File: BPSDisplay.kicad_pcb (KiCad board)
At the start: 2 copper layers, 85 x 56 mm, 61 parts, among them J1 SWD, J3 CAN_Out, J4 CAN_Out, J5 CarPowerConnector, J6 CAN_LogicAnalyzer, J7 SPI0_LogicAnalyzer, J8 GEN_LogicAnalyzer, J9 USART_LogicAnalyzer, P1 Conn_02x20_Odd_Even, SW1 Reset, U1 STM32F413RHTx, U2 ADM3055E, U3 CDSOT23-T24CAN, U6 PDS1-S12-S5, U7 NCP1117-3.3_SOT223, Y1 8M

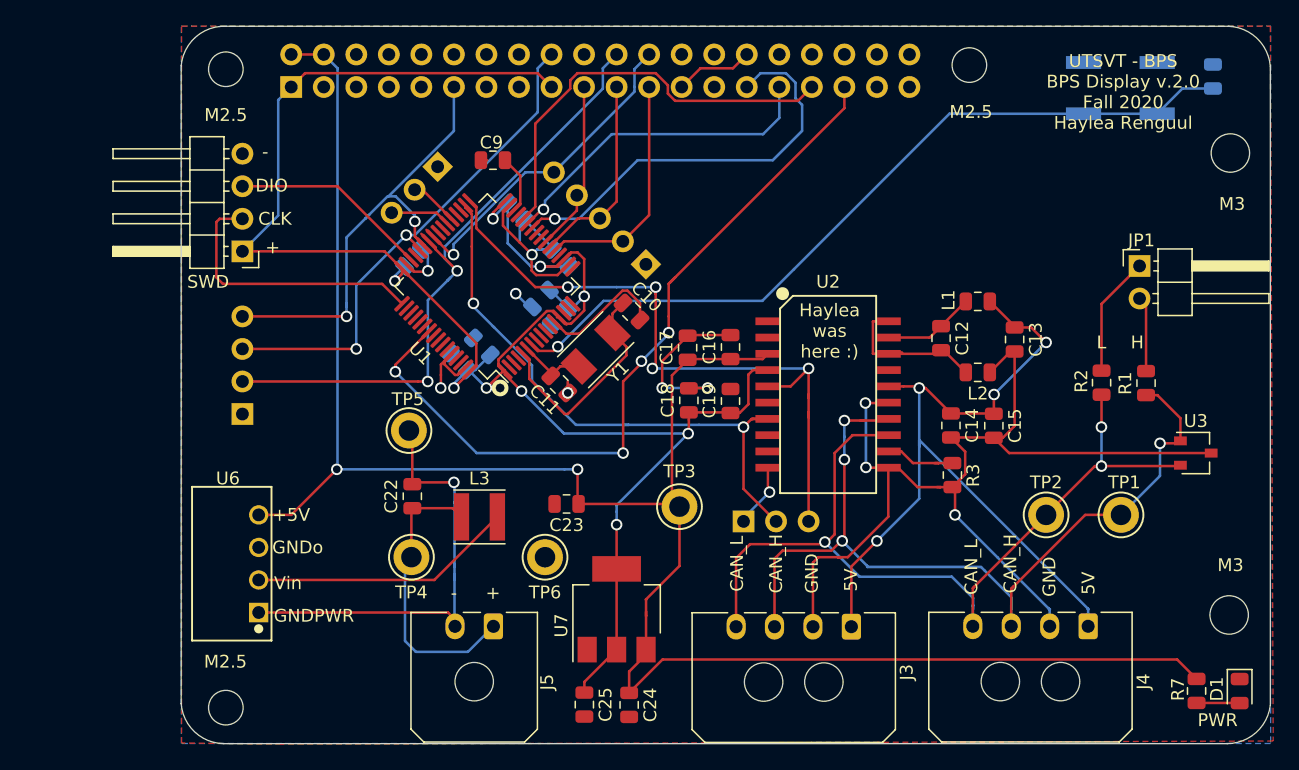
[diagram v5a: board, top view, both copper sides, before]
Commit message: Adds LED for supplementals, deletes unncessary files, and links all symbols to the submodule
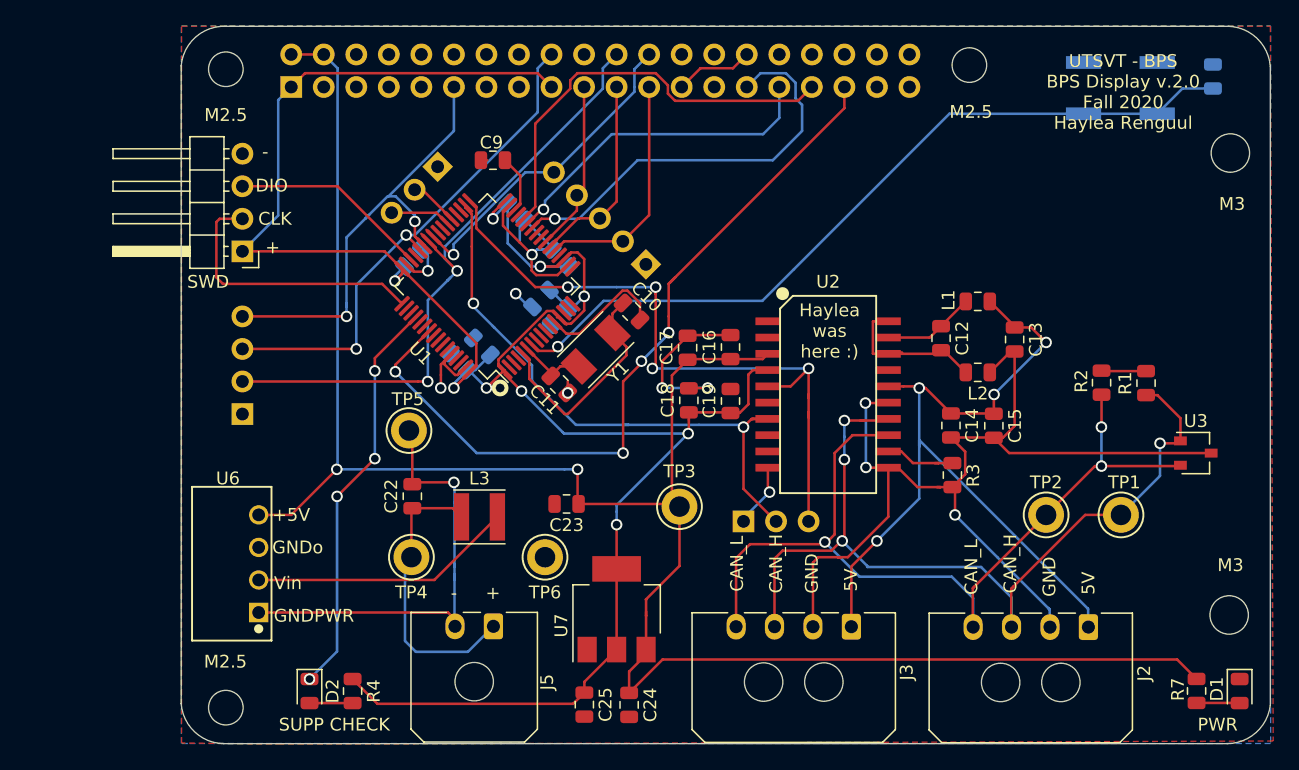
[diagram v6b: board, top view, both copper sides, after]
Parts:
- removed J4: CAN_Out, Connector_Molex:Molex_Micro-Fit_3.0_43650-0400_1x04_P3.00mm_Horizontal
- removed JP1: Termination Resistors, Connector_PinHeader_2.54mm:PinHeader_1x02_P2.54mm_Horizontal
- added D2: PowerOn, LED_SMD:LED_0805_2012Metric, F.Cu at (206.0, 156.9)
- added J2: CAN_Out, Connector_Molex:Molex_Micro-Fit_3.0_43650-0400_1x04_P3.00mm_Horizontal, F.Cu at (266.8, 151.9)
- added R4: 750, Resistor_SMD:R_0805_2012Metric, F.Cu at (209.4, 156.9)
- LOGO1: value Logo_Placeholder -> UTSVT
- LOGO2: value Logo_Placeholder -> Dr. Hallock
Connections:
- P1 pad 10: (no net) -> Net-(P1-Pad10)
- P1 pad 12: (no net) -> Net-(P1-Pad12)
- P1 pad 13: (no net) -> Net-(P1-Pad13)
- P1 pad 15: (no net) -> Net-(P1-Pad15)
- P1 pad 16: (no net) -> Net-(P1-Pad16)
- P1 pad 26: (no net) -> Net-(P1-Pad26)
- P1 pad 27: (no net) -> Net-(P1-Pad27)
- P1 pad 28: (no net) -> Net-(P1-Pad28)
- P1 pad 3: (no net) -> Net-(P1-Pad3)
- P1 pad 32: (no net) -> Net-(P1-Pad32)
- P1 pad 36: (no net) -> Net-(P1-Pad36)
- P1 pad 37: (no net) -> Net-(P1-Pad37)
- P1 pad 38: (no net) -> Net-(P1-Pad38)
- P1 pad 40: (no net) -> Net-(P1-Pad40)
- P1 pad 5: (no net) -> Net-(P1-Pad5)
- P1 pad 7: (no net) -> Net-(P1-Pad7)
- P1 pad 8: (no net) -> Net-(P1-Pad8)
- R1 pad 1: /CAN/TERM_H -> Net-(R1-Pad1)
- R2 pad 1: /CAN/TERM_L -> Net-(R1-Pad1)
- U1 pad 10: (no net) -> Net-(U1-Pad10)
- U1 pad 11: (no net) -> Net-(U1-Pad11)
- U1 pad 14: (no net) -> Net-(U1-Pad14)
- U1 pad 15: (no net) -> Net-(U1-Pad15)
- U1 pad 16: (no net) -> Net-(U1-Pad16)
- U1 pad 17: (no net) -> Net-(U1-Pad17)
- U1 pad 2: (no net) -> Net-(U1-Pad2)
- U1 pad 20: (no net) -> Net-(U1-Pad20)
- U1 pad 24: (no net) -> Net-(U1-Pad24)
- U1 pad 25: (no net) -> Net-(U1-Pad25)
- U1 pad 29: (no net) -> Net-(U1-Pad29)
- U1 pad 3: (no net) -> Net-(U1-Pad3)
- U1 pad 35: (no net) -> Net-(U1-Pad35)
- U1 pad 36: (no net) -> Net-(U1-Pad36)
- U1 pad 39: (no net) -> Net-(U1-Pad39)
- U1 pad 4: (no net) -> Net-(U1-Pad4)
- U1 pad 40: (no net) -> Net-(U1-Pad40)
- U1 pad 45: (no net) -> Net-(U1-Pad45)
- U1 pad 50: (no net) -> Net-(U1-Pad50)
- U1 pad 51: (no net) -> Net-(U1-Pad51)
- U1 pad 52: (no net) -> Net-(D2-Pad1)
- U1 pad 53: (no net) -> Net-(U1-Pad53)
- U1 pad 54: (no net) -> Net-(U1-Pad54)
- U1 pad 56: (no net) -> Net-(U1-Pad56)
- U1 pad 57: (no net) -> Net-(U1-Pad57)
- U1 pad 58: (no net) -> Net-(U1-Pad58)
- U1 pad 59: (no net) -> Net-(U1-Pad59)
- U1 pad 61: (no net) -> Net-(U1-Pad61)
- U1 pad 62: (no net) -> Net-(U1-Pad62)
- U1 pad 8: (no net) -> Net-(U1-Pad8)
- U1 pad 9: (no net) -> Net-(U1-Pad9)
- U2 pad 17: (no net) -> Net-(U2-Pad17)
- U2 pad 6: (no net) -> Net-(U2-Pad6)
- U2 pad 8: (no net) -> Net-(U2-Pad8)
- U2 pad 9: (no net) -> Net-(U2-Pad9)
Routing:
- net Net-(D2-Pad1): track 0.00 -> 31.7 mm, vias 0 -> 4
- net +3V3: track 159.9 -> 179.2 mm
- net /CAN/TERM_L: track 9.70 -> 0.00 mm
- net /CAN/TERM_H: track 5.88 -> 0.00 mm
- net Net-(R1-Pad1): track 0.00 -> 3.49 mm
- net Net-(D2-Pad2): track 0.00 -> 3.36 mm
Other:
- board text added: "SUPP CHECK"
- board text removed: "H"
- board text removed: "L"

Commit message: Redo most of the layout to fix issues.
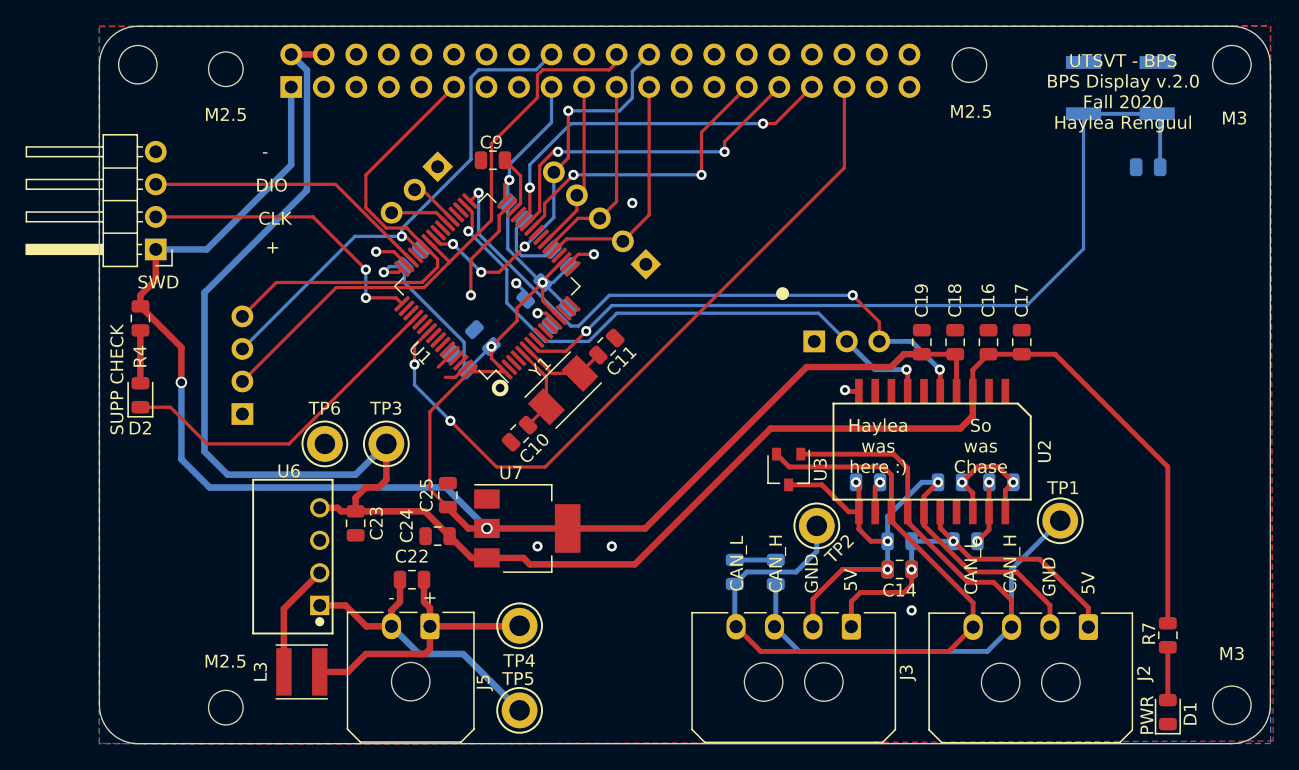
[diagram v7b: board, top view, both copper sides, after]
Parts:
- added MK6: M3, MountingHole:MountingHole_3mm, F.Cu at (192.6, 108.0)
- C12, C13, C15, L1, L2, R1, R2, R3: moved to B.Cu
- moved R4 33.5 mm to (192.8, 127.8)
- moved LOGO1 33.1 mm to (257.6, 135.8)
- moved R1 32.4 mm to (242.4, 147.6)
- moved R2 32.2 mm to (239.2, 147.6)
- moved U3 31.8 mm to (243.4, 139.6), turned to 270 degrees
- moved D2 26.6 mm to (192.8, 133.8), turned to 90 degrees
- moved C17 26.1 mm to (261.6, 129.7)
- moved TP5 23.5 mm to (222.4, 158.4)
- moved TP3 23.4 mm to (212.0, 137.6)
- moved C18 21.3 mm to (256.4, 129.7)
- moved C16 20.1 mm to (259.0, 129.7)
- moved C24 19.9 mm to (216.0, 144.8), turned to 180 degrees
- moved C25 19.5 mm to (216.8, 141.6), turned to 90 degrees
- moved TP6 19.3 mm to (207.2, 137.6), turned to 0 degrees
- moved L1 18.7 mm to (257.2, 145.2), turned to 0 degrees
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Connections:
- P1 pad 10: Net-(P1-Pad10) -> (no net)
- P1 pad 12: Net-(P1-Pad12) -> (no net)
- P1 pad 13: Net-(P1-Pad13) -> (no net)
- P1 pad 15: Net-(P1-Pad15) -> (no net)
- P1 pad 16: Net-(P1-Pad16) -> (no net)
- P1 pad 26: Net-(P1-Pad26) -> (no net)
- P1 pad 27: Net-(P1-Pad27) -> (no net)
- P1 pad 28: Net-(P1-Pad28) -> (no net)
- P1 pad 3: Net-(P1-Pad3) -> (no net)
- P1 pad 32: Net-(P1-Pad32) -> (no net)
- P1 pad 36: Net-(P1-Pad36) -> (no net)
- P1 pad 37: Net-(P1-Pad37) -> (no net)
- P1 pad 38: Net-(P1-Pad38) -> (no net)
- P1 pad 40: Net-(P1-Pad40) -> (no net)
- P1 pad 5: Net-(P1-Pad5) -> (no net)
- P1 pad 7: Net-(P1-Pad7) -> (no net)
- P1 pad 8: Net-(P1-Pad8) -> (no net)
- U1 pad 10: Net-(U1-Pad10) -> (no net)
- U1 pad 11: Net-(U1-Pad11) -> (no net)
- U1 pad 14: Net-(U1-Pad14) -> (no net)
- U1 pad 15: Net-(U1-Pad15) -> (no net)
- U1 pad 16: Net-(U1-Pad16) -> (no net)
- U1 pad 17: Net-(U1-Pad17) -> (no net)
- U1 pad 2: Net-(U1-Pad2) -> (no net)
- U1 pad 20: Net-(U1-Pad20) -> (no net)
- U1 pad 24: Net-(U1-Pad24) -> (no net)
- U1 pad 25: Net-(U1-Pad25) -> (no net)
- U1 pad 29: Net-(U1-Pad29) -> (no net)
- U1 pad 3: Net-(U1-Pad3) -> (no net)
- U1 pad 35: Net-(U1-Pad35) -> (no net)
- U1 pad 36: Net-(U1-Pad36) -> (no net)
- U1 pad 39: Net-(U1-Pad39) -> (no net)
- U1 pad 4: Net-(U1-Pad4) -> (no net)
- U1 pad 40: Net-(U1-Pad40) -> (no net)
- U1 pad 45: Net-(U1-Pad45) -> (no net)
- U1 pad 50: Net-(U1-Pad50) -> (no net)
- U1 pad 51: Net-(U1-Pad51) -> (no net)
- U1 pad 53: Net-(U1-Pad53) -> (no net)
- U1 pad 54: Net-(U1-Pad54) -> (no net)
- U1 pad 56: Net-(U1-Pad56) -> (no net)
- U1 pad 57: Net-(U1-Pad57) -> (no net)
- U1 pad 58: Net-(U1-Pad58) -> (no net)
- U1 pad 59: Net-(U1-Pad59) -> (no net)
- U1 pad 61: Net-(U1-Pad61) -> (no net)
- U1 pad 62: Net-(U1-Pad62) -> (no net)
- U1 pad 8: Net-(U1-Pad8) -> (no net)
- U1 pad 9: Net-(U1-Pad9) -> (no net)
- U2 pad 17: Net-(U2-Pad17) -> (no net)
- U2 pad 6: Net-(U2-Pad6) -> (no net)
- U2 pad 8: Net-(U2-Pad8) -> (no net)
- U2 pad 9: Net-(U2-Pad9) -> (no net)
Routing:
- net GND: track 68.4 -> 26.9 mm, vias 8 -> 10
- net Net-(C13-Pad2): track 82.3 -> 48.8 mm, vias 3 -> 4
- net Net-(C13-Pad1): track 63.4 -> 30.8 mm, vias 4 -> 2
- net /CAN/CAN_L: track 69.3 -> 57.1 mm, vias 3 -> 0
- net Net-(L3-Pad2): track 20.7 -> 8.89 mm
- net Net-(C10-Pad1): track 18.6 -> 6.94 mm
- net GNDPWR: track 34.1 -> 22.9 mm, vias 1 -> 0
- net /CAN/CAN_H: track 69.5 -> 59.1 mm, vias 4 -> 0
- net /GPIO5: track 32.8 -> 23.8 mm, vias 1 -> 2
- net /SWDIO: track 15.6 -> 22.4 mm
- net /GPIO19: track 61.9 -> 56.9 mm, vias 4 -> 2
- net Net-(D2-Pad1): track 31.7 -> 26.8 mm, vias 4 -> 0
- net /NRST: track 62.3 -> 67.1 mm
- net +3V3: track 179.2 -> 183.6 mm, vias 9 -> 6
- net /CAN2_RX: track 53.4 -> 49.1 mm, vias 4 -> 3
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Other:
- board size 85 x 56 mm -> 91.4 x 56 mm
- rule via_min_drill: 0.5 -> 0.3
- rule via_min_size: 0.8 -> 0.6
- board text added: "So was Chase"
- board text removed: "+5V"
- board text removed: "GNDPWR"
- board text removed: "GNDo"
- board text removed: "Vin"

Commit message: Adds another mounting hole, moves PWR LED, and adds labels to test points
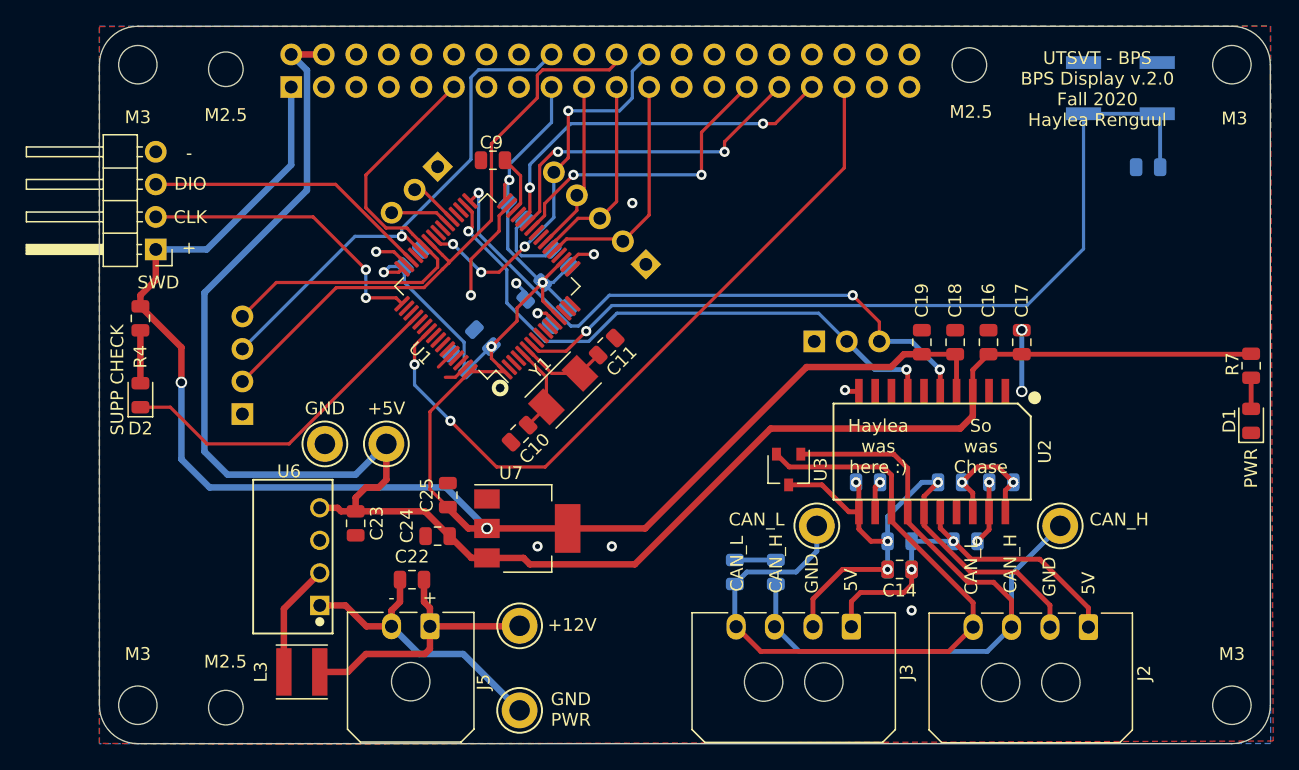
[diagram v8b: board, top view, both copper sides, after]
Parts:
- added MK7: M3, MountingHole:MountingHole_3mm, F.Cu at (192.6, 158.0)
- moved D1 23.6 mm to (279.5, 135.8)
- moved R7 22.0 mm to (279.5, 131.5)
- moved LOGO1 17.4 mm to (273.9, 141.8), turned to 270 degrees
- moved LOGO2 12.3 mm to (270.0, 122.5), turned to 270 degrees
- moved TP1 0.40 mm to (264.6, 144.0)
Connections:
- P1 pad 10: (no net) -> Net-(P1-Pad10)
- P1 pad 12: (no net) -> Net-(P1-Pad12)
- P1 pad 13: (no net) -> Net-(P1-Pad13)
- P1 pad 15: (no net) -> Net-(P1-Pad15)
- P1 pad 16: (no net) -> Net-(P1-Pad16)
- P1 pad 26: (no net) -> Net-(P1-Pad26)
- P1 pad 27: (no net) -> Net-(P1-Pad27)
- P1 pad 28: (no net) -> Net-(P1-Pad28)
- P1 pad 3: (no net) -> Net-(P1-Pad3)
- P1 pad 32: (no net) -> Net-(P1-Pad32)
- P1 pad 36: (no net) -> Net-(P1-Pad36)
- P1 pad 37: (no net) -> Net-(P1-Pad37)
- P1 pad 38: (no net) -> Net-(P1-Pad38)
- P1 pad 40: (no net) -> Net-(P1-Pad40)
- P1 pad 5: (no net) -> Net-(P1-Pad5)
- P1 pad 7: (no net) -> Net-(P1-Pad7)
- P1 pad 8: (no net) -> Net-(P1-Pad8)
- U1 pad 10: (no net) -> Net-(U1-Pad10)
- U1 pad 11: (no net) -> Net-(U1-Pad11)
- U1 pad 14: (no net) -> Net-(U1-Pad14)
- U1 pad 15: (no net) -> Net-(U1-Pad15)
- U1 pad 16: (no net) -> Net-(U1-Pad16)
- U1 pad 17: (no net) -> Net-(U1-Pad17)
- U1 pad 2: (no net) -> Net-(U1-Pad2)
- U1 pad 20: (no net) -> Net-(U1-Pad20)
- U1 pad 24: (no net) -> Net-(U1-Pad24)
- U1 pad 25: (no net) -> Net-(U1-Pad25)
- U1 pad 29: (no net) -> Net-(U1-Pad29)
- U1 pad 3: (no net) -> Net-(U1-Pad3)
- U1 pad 35: (no net) -> Net-(U1-Pad35)
- U1 pad 36: (no net) -> Net-(U1-Pad36)
- U1 pad 39: (no net) -> Net-(U1-Pad39)
- U1 pad 4: (no net) -> Net-(U1-Pad4)
- U1 pad 40: (no net) -> Net-(U1-Pad40)
- U1 pad 45: (no net) -> Net-(U1-Pad45)
- U1 pad 50: (no net) -> Net-(U1-Pad50)
- U1 pad 51: (no net) -> Net-(U1-Pad51)
- U1 pad 53: (no net) -> Net-(U1-Pad53)
- U1 pad 54: (no net) -> Net-(U1-Pad54)
- U1 pad 56: (no net) -> Net-(U1-Pad56)
- U1 pad 57: (no net) -> Net-(U1-Pad57)
- U1 pad 58: (no net) -> Net-(U1-Pad58)
- U1 pad 59: (no net) -> Net-(U1-Pad59)
- U1 pad 61: (no net) -> Net-(U1-Pad61)
- U1 pad 62: (no net) -> Net-(U1-Pad62)
- U1 pad 8: (no net) -> Net-(U1-Pad8)
- U1 pad 9: (no net) -> Net-(U1-Pad9)
- U2 pad 17: (no net) -> Net-(U2-Pad17)
- U2 pad 6: (no net) -> Net-(U2-Pad6)
- U2 pad 8: (no net) -> Net-(U2-Pad8)
- U2 pad 9: (no net) -> Net-(U2-Pad9)
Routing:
- net +5V: track 152.9 -> 143.6 mm
- net GND: track 26.9 -> 31.7 mm, vias 10 -> 12
- net Net-(D1-Pad2): track 4.12 -> 2.43 mm
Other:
- board text added: "+12V"
- board text added: "+5V"
- board text added: "Dr. Gary Hallock"
- board text added: "GND PWR"
